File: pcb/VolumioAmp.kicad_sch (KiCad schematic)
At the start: 0 parts

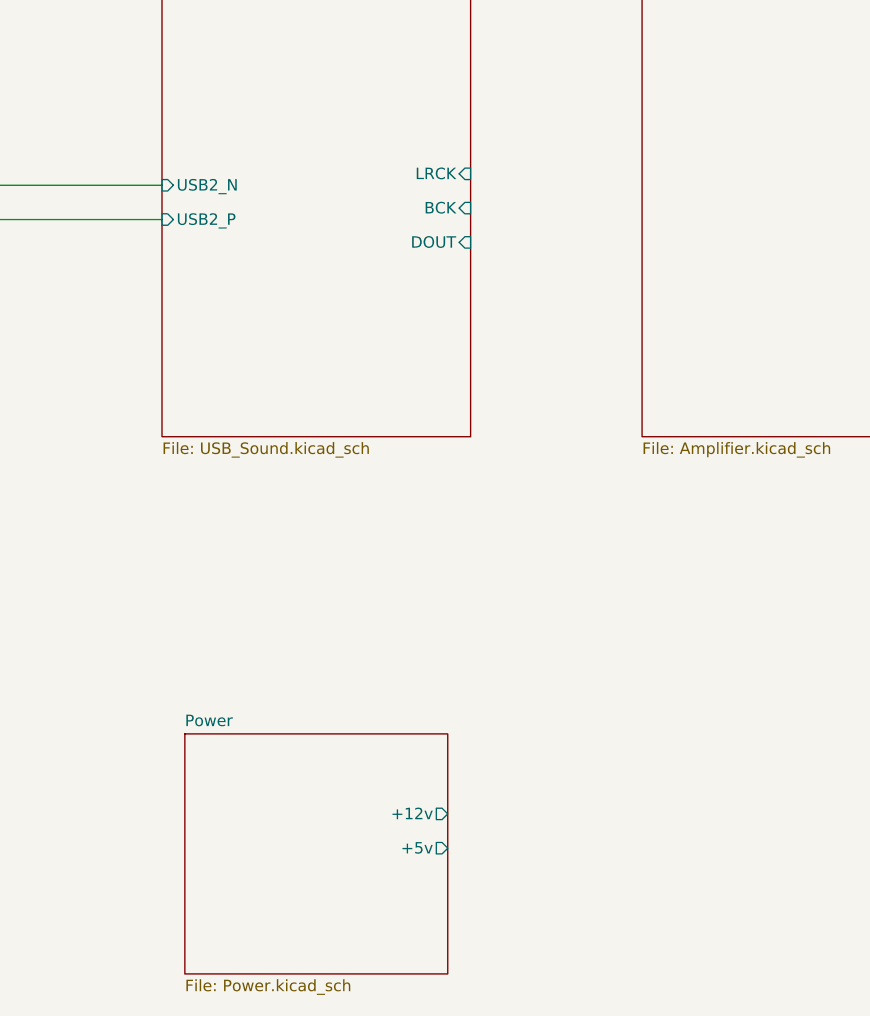
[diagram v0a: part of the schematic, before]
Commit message: - USB sound wired
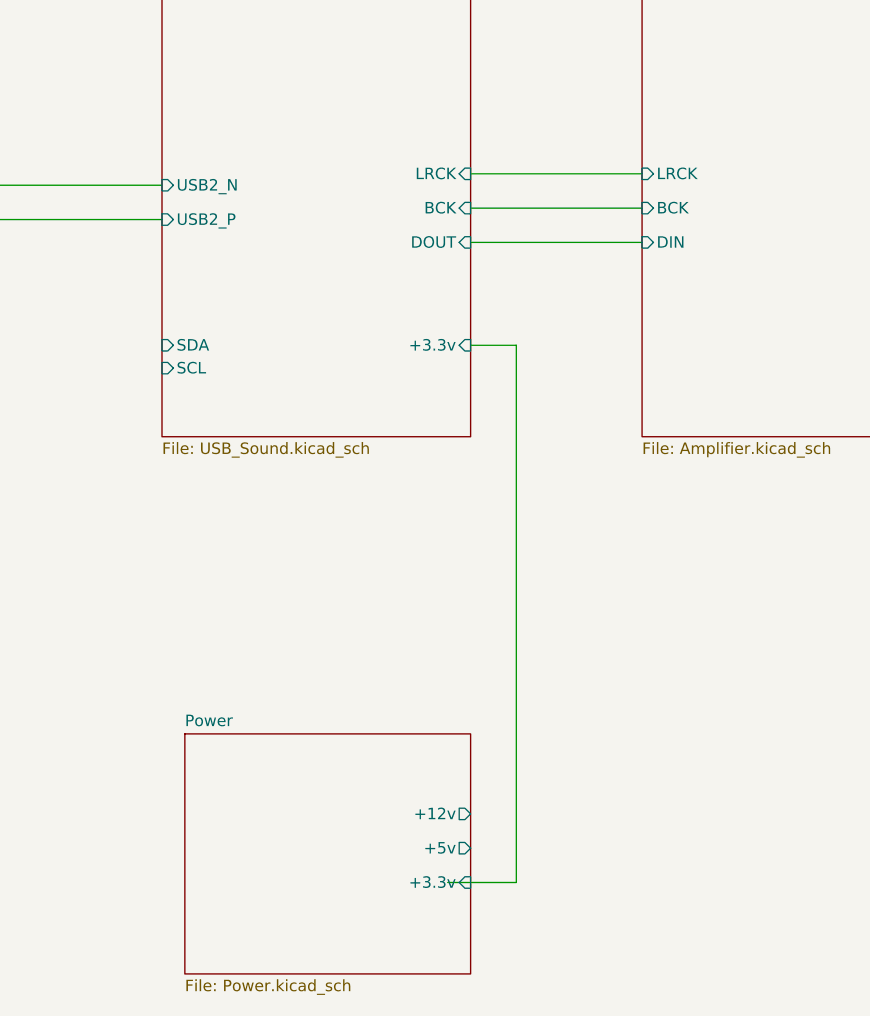
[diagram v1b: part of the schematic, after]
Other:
- sheet Amplifier ports: added BCK, DIN, LRCK; removed none
- sheet Power ports: added +3.3v; removed none
- sheet USB_Sound ports: added +3.3v, SCL, SDA; removed none
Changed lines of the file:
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@@
 (kicad_sch (version 20230121) (generator eeschema)
   (paper "A4")
+  (wire (pts (xy 154.94 80.01) (xy 154.94 139.7))
+    (stroke (width 0) (type default))
+  )
   (wire (pts (xy 82.55 66.04) (xy 115.57 66.04))
     (stroke (width 0) (type default))
   )
+  (wire (pts (xy 149.86 80.01) (xy 154.94 80.01))
+    (stroke (width 0) (type default))
+  )
+  (wire (pts (xy 149.86 64.77) (xy 168.91 64.77))
+    (stroke (width 0) (type default))
+  )
+  (wire (pts (xy 149.86 60.96) (xy 168.91 60.96))
+    (stroke (width 0) (type default))
+  )
+  (wire (pts (xy 154.94 139.7) (xy 147.32 139.7))
+    (stroke (width 0) (type default))
+  )
   (wire (pts (xy 82.55 62.23) (xy 115.57 62.23))
+    (stroke (width 0) (type default))
+  )
+  (wire (pts (xy 149.86 68.58) (xy 168.91 68.58))
     (stroke (width 0) (type default))
   )
@@
       (effects (font (size 1.27 1.27)) (justify right))
     )
+    (pin "+3.3v" input (at 149.86 80.01 0)
+      (effects (font (size 1.27 1.27)) (justify right))
+    )
+    (pin "SDA" input (at 115.57 80.01 180)
+      (effects (font (size 1.27 1.27)) (justify left))
+    )
+    (pin "SCL" input (at 115.57 82.55 180)
+      (effects (font (size 1.27 1.27)) (justify left))
+    )
     (instances
       (project "VolumioAmp"
@@
     )
   )
-  (sheet (at 118.11 123.19) (size 29.21 26.67) (fields_autoplaced)
+  (sheet (at 118.11 123.19) (size 31.75 26.67) (fields_autoplaced)
     (stroke (width 0.1524) (type solid))
     (fill (color 0 0 0 0.0000))
@@
       (effects (font (size 1.27 1.27)) (justify left top))
     )
-    (pin "+12v" output (at 147.32 132.08 0)
+    (pin "+12v" output (at 149.86 132.08 0)
       (effects (font (size 1.27 1.27)) (justify right))
     )
-    (pin "+5v" output (at 147.32 135.89 0)
+    (pin "+5v" output (at 149.86 135.89 0)
+      (effects (font (size 1.27 1.27)) (justify right))
+    )
+    (pin "+3.3v" input (at 149.86 139.7 0)
       (effects (font (size 1.27 1.27)) (justify right))
     )
@@
       (effects (font (size 1.27 1.27)) (justify left top))
     )
+    (pin "LRCK" input (at 168.91 60.96 180)
+      (effects (font (size 1.27 1.27)) (justify left))
+    )
+    (pin "BCK" input (at 168.91 64.77 180)
+      (effects (font (size 1.27 1.27)) (justify left))
+    )
+    (pin "DIN" input (at 168.91 68.58 180)
+      (effects (font (size 1.27 1.27)) (justify left))
+    )
     (instances

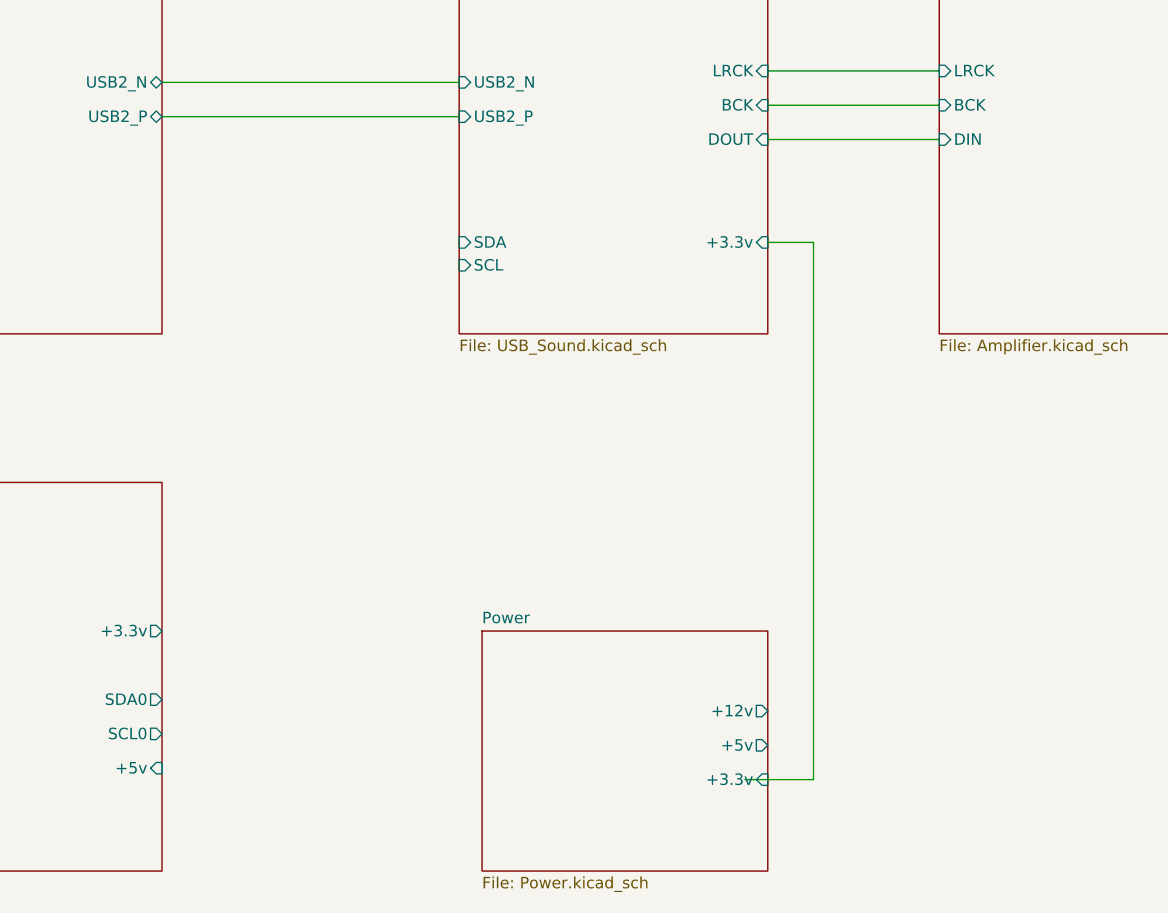
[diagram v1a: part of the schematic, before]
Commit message: WM8804 via i2c
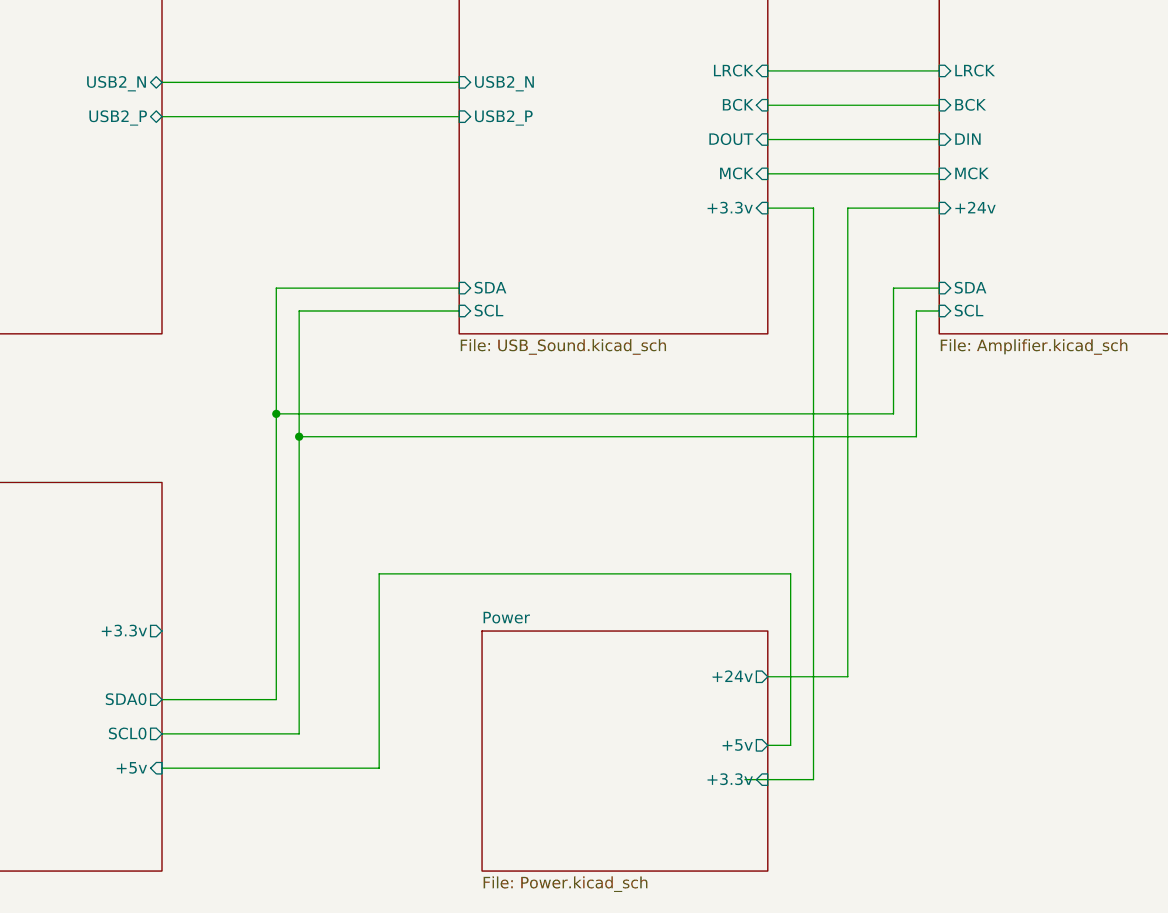
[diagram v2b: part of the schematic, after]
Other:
- sheet Amplifier ports: added +24v, MCK, SCL, SDA; removed none
- sheet Power ports: added +24v; removed +12v
- sheet USB_Sound ports: added MCK; removed none
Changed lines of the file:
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@@
 (kicad_sch (version 20230121) (generator eeschema)
   (paper "A4")
-  (wire (pts (xy 154.94 80.01) (xy 154.94 139.7))
+  (junction (at 97.79 101.6) (diameter 0) (color 0 0 0 0)
+  )
+  (junction (at 95.25 99.06) (diameter 0) (color 0 0 0 0)
+  )
+  (wire (pts (xy 168.91 85.09) (xy 163.83 85.09))
+    (stroke (width 0) (type default))
+  )
+  (wire (pts (xy 95.25 85.09) (xy 115.57 85.09))
+    (stroke (width 0) (type default))
+  )
+  (wire (pts (xy 154.94 76.2) (xy 154.94 139.7))
     (stroke (width 0) (type default))
   )
@@
     (stroke (width 0) (type default))
   )
-  (wire (pts (xy 149.86 80.01) (xy 154.94 80.01))
+  (wire (pts (xy 149.86 76.2) (xy 154.94 76.2))
+    (stroke (width 0) (type default))
+  )
+  (wire (pts (xy 152.4 135.89) (xy 152.4 116.84))
     (stroke (width 0) (type default))
   )
@@
     (stroke (width 0) (type default))
   )
+  (wire (pts (xy 97.79 134.62) (xy 82.55 134.62))
+    (stroke (width 0) (type default))
+  )
   (wire (pts (xy 149.86 60.96) (xy 168.91 60.96))
     (stroke (width 0) (type default))
   )
+  (wire (pts (xy 95.25 99.06) (xy 95.25 85.09))
+    (stroke (width 0) (type default))
+  )
+  (wire (pts (xy 166.37 87.63) (xy 166.37 101.6))
+    (stroke (width 0) (type default))
+  )
+  (wire (pts (xy 82.55 138.43) (xy 106.68 138.43))
+    (stroke (width 0) (type default))
+  )
+  (wire (pts (xy 152.4 116.84) (xy 106.68 116.84))
+    (stroke (width 0) (type default))
+  )
+  (wire (pts (xy 168.91 76.2) (xy 158.75 76.2))
+    (stroke (width 0) (type default))
+  )
+  (wire (pts (xy 163.83 99.06) (xy 95.25 99.06))
+    (stroke (width 0) (type default))
+  )
+  (wire (pts (xy 115.57 87.63) (xy 97.79 87.63))
+    (stroke (width 0) (type default))
+  )
+  (wire (pts (xy 163.83 85.09) (xy 163.83 99.06))
+    (stroke (width 0) (type default))
+  )
+  (wire (pts (xy 97.79 101.6) (xy 97.79 134.62))
+    (stroke (width 0) (type default))
+  )
+  (wire (pts (xy 149.86 135.89) (xy 152.4 135.89))
+    (stroke (width 0) (type default))
+  )
+  (wire (pts (xy 149.86 72.39) (xy 168.91 72.39))
+    (stroke (width 0) (type default))
+  )
+  (wire (pts (xy 82.55 130.81) (xy 95.25 130.81))
+    (stroke (width 0) (type default))
+  )
+  (wire (pts (xy 97.79 87.63) (xy 97.79 101.6))
+    (stroke (width 0) (type default))
+  )
   (wire (pts (xy 154.94 139.7) (xy 147.32 139.7))
     (stroke (width 0) (type default))
   )
+  (wire (pts (xy 158.75 128.27) (xy 149.86 128.27))
+    (stroke (width 0) (type default))
+  )
+  (wire (pts (xy 106.68 116.84) (xy 106.68 138.43))
+    (stroke (width 0) (type default))
+  )
+  (wire (pts (xy 168.91 87.63) (xy 166.37 87.63))
+    (stroke (width 0) (type default))
+  )
+  (wire (pts (xy 95.25 130.81) (xy 95.25 99.06))
+    (stroke (width 0) (type default))
+  )
   (wire (pts (xy 82.55 62.23) (xy 115.57 62.23))
     (stroke (width 0) (type default))
   )
+  (wire (pts (xy 158.75 76.2) (xy 158.75 128.27))
+    (stroke (width 0) (type default))
+  )
   (wire (pts (xy 149.86 68.58) (xy 168.91 68.58))
     (stroke (width 0) (type default))
   )
+  (wire (pts (xy 166.37 101.6) (xy 97.79 101.6))
+    (stroke (width 0) (type default))
+  )
   (sheet (at 38.1 106.68) (size 44.45 43.18) (fields_autoplaced)
     (stroke (width 0.1524) (type solid))
@@
       (effects (font (size 1.27 1.27)) (justify right))
     )
-    (pin "+3.3v" input (at 149.86 80.01 0)
-      (effects (font (size 1.27 1.27)) (justify right))
-    )
-    (pin "SDA" input (at 115.57 80.01 180)
-      (effects (font (size 1.27 1.27)) (justify left))
-    )
-    (pin "SCL" input (at 115.57 82.55 180)
-      (effects (font (size 1.27 1.27)) (justify left))
+    (pin "+3.3v" input (at 149.86 76.2 0)
+      (effects (font (size 1.27 1.27)) (justify right))
+    )
+    (pin "SDA" input (at 115.57 85.09 180)
+      (effects (font (size 1.27 1.27)) (justify left))
+    )
+    (pin "SCL" input (at 115.57 87.63 180)
+      (effects (font (size 1.27 1.27)) (justify left))
+    )
+    (pin "MCK" input (at 149.86 72.39 0)
+      (effects (font (size 1.27 1.27)) (justify right))
     )
     (instances
@@
       (effects (font (size 1.27 1.27)) (justify left top))
     )
-    (pin "+12v" output (at 149.86 132.08 0)
-      (effects (font (size 1.27 1.27)) (justify right))
-    )
     (pin "+5v" output (at 149.86 135.89 0)
       (effects (font (size 1.27 1.27)) (justify right))
@@
       (effects (font (size 1.27 1.27)) (justify right))
     )
+    (pin "+24v" output (at 149.86 128.27 0)
+      (effects (font (size 1.27 1.27)) (justify right))
+    )
     (instances
       (project "VolumioAmp"
@@
       (effects (font (size 1.27 1.27)) (justify left))
     )
+    (pin "MCK" input (at 168.91 72.39 180)
+      (effects (font (size 1.27 1.27)) (justify left))
+    )
+    (pin "+24v" input (at 168.91 76.2 180)
+      (effects (font (size 1.27 1.27)) (justify left))
+    )
+    (pin "SDA" input (at 168.91 85.09 180)
+      (effects (font (size 1.27 1.27)) (justify left))
+    )
+    (pin "SCL" input (at 168.91 87.63 180)
+      (effects (font (size 1.27 1.27)) (justify left))
+    )

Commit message: - work in progress
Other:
- added sheet I2STest (I2STest.kicad_sch)
- sheet Amplifier ports: added I2S; removed BCK, DIN, LRCK, MCK
- sheet CM4_Ethernet ports: added I2S; removed none
- sheet USB_Sound ports: added I2S; removed BCK, DOUT, LRCK, MCK
